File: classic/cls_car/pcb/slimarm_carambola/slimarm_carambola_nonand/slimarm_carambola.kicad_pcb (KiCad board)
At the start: 4 copper layers, 42 x 25.6 mm, 74 parts, among them J1 USB_C_Receptacle_USB2.0, J2 Conn_01x05, J3 Conn_01x04, J4 Conn_01x04, U1 AT91SAM9G25-CU, U2 16bit-DDR2-8bank-FBGA84, U3 W25Q128JVS, U5 XC6206PxxxMR, U6 XC6206PxxxMR, U7 XC6206PxxxMR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

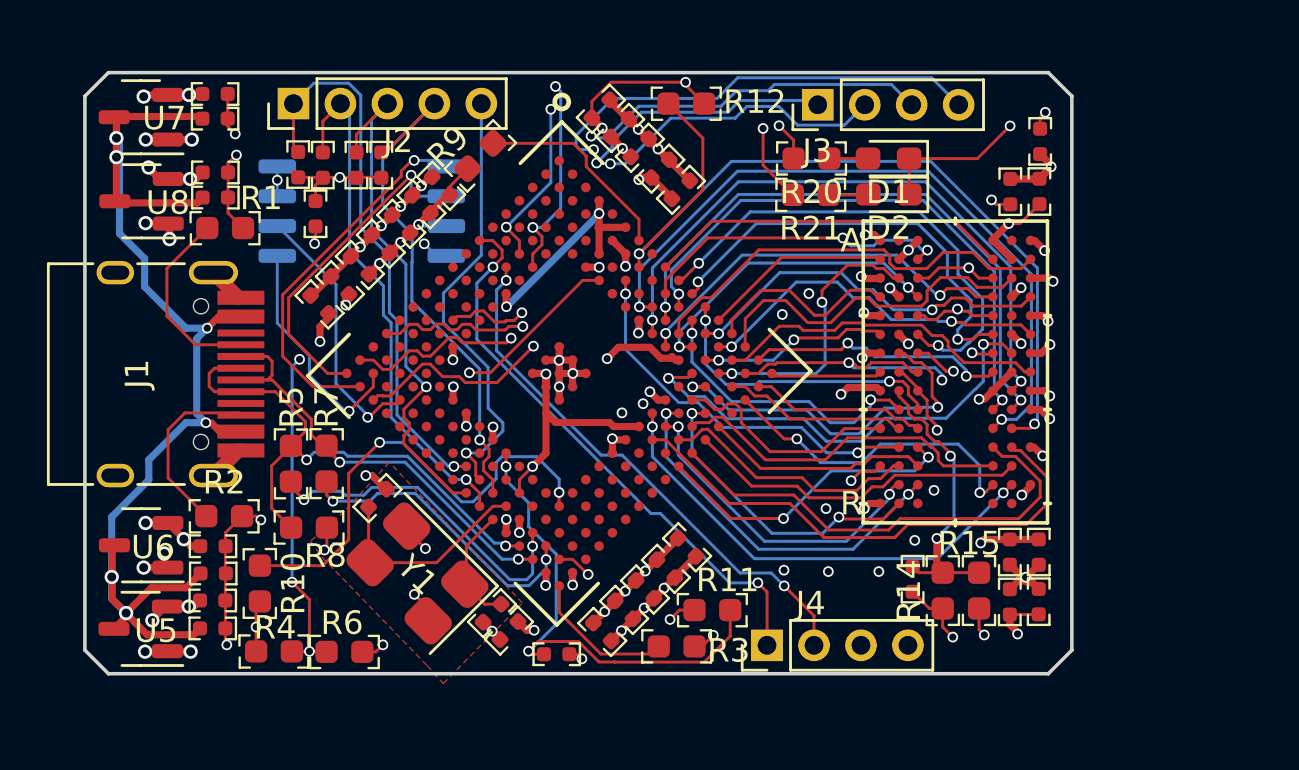
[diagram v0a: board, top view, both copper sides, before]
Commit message: fixed carambola board; board 3d models
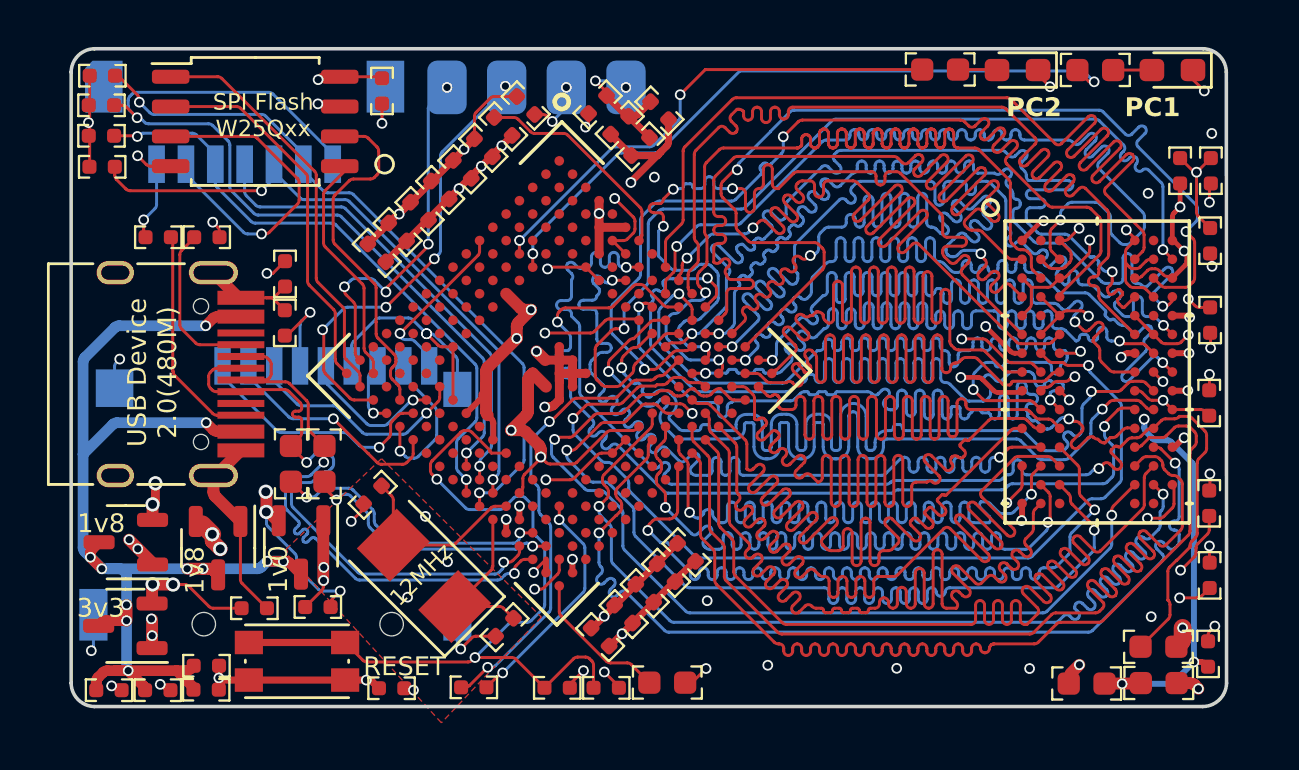
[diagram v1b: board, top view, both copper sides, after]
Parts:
- removed C17, C18: 100nF, jlywxy:0402
- removed J3: Conn_01x04, Connector_PinHeader_2.00mm:PinHeader_1x04_P2.00mm_Vertical
- removed R16, R17, R18, R19: 10k, jlywxy:0402
- removed R4: NC, jlywxy:0603
- removed R6: 0, jlywxy:0603
- removed R8: 1.5k, jlywxy:0603
- added C28: 100nF, jlywxy:0402, F.Cu at (24.9, 25.1)
- added G***: LOGO, jlywxy:image_microchip, B.Cu at (27.6, 20.6)
- added R13: 10k, jlywxy:0402, F.Cu at (17.1, 15.9)
- added R22: 10k, jlywxy:0402, F.Cu at (17.1, 14.6)
- added R23: 10k, jlywxy:0402, F.Cu at (17.1, 18.5)
- added R24: 10k, jlywxy:0402, F.Cu at (17.1, 17.2)
- added SW1: SW_MEC_5E, jlywxy:BUTTON_4P_3x4, F.Cu at (25.4, 39.5)
- added U4: ~, jlywxy:MicroSD-TF_PUSH-SHOUHAN, B.Cu at (33.6, 25.5)
- J2: value Conn_01x05 -> Conn_01x04; footprint Connector_PinHeader_2.00mm:PinHeader_1x05_P2.00mm_Vertical -> Connector_PinHeader_2.54mm:PinHeader_1x04_P2.54mm_Vertical; moved to B.Cu
- J4: value Conn_01x04 -> DF13A-7P-1.25H21; footprint Connector_PinHeader_2.00mm:PinHeader_1x04_P2.00mm_Vertical -> jlywxy:DF13A-7P-1.25H21; moved to B.Cu
- R1, R2, R9: footprint jlywxy:0603 -> jlywxy:0402
- R10, R11: value 1.5k -> 5.1k; footprint jlywxy:0603 -> jlywxy:0402
- U3: moved to F.Cu
- Y1: value Crystal_GND24 -> Crystal; footprint jlywxy:Crystal_5032-4P -> Crystal:Crystal_SMD_5032-2Pin_5.0x3.2mm
- moved R12 30.6 mm to (62.1, 38.9)
- moved G*** 28.2 mm to (20.0, 20.7)
- moved J4 27.6 mm to (26.9, 18.4), turned to 0 degrees
- moved C38 26.4 mm to (29.4, 40.7), turned to 0 degrees
- moved G*** 25.7 mm to (27.7, 23.7)
- moved C39 23.3 mm to (21.6, 39.7)
- moved C37 21.0 mm to (21.6, 40.8)
- moved C40 19.0 mm to (26.3, 37.2), turned to 0 degrees
- moved U7 18.6 mm to (22.1, 34.7), turned to -90 degrees
- moved C24 18.4 mm to (64.3, 35.9)
- moved U8 16.2 mm to (25.6, 34.7), turned to -90 degrees
- moved C19 15.1 mm to (64.3, 21.6)
- moved C11 14.9 mm to (39.2, 16.7), turned to -135 degrees
- moved J2 14.2 mm to (39.4, 15.1)
- moved C20 13.1 mm to (64.3, 25.0)
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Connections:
- net /DDR_CLK renamed /DDR_CLKP
- net /DDR_NCLK renamed /DDR_CLKN
- J2 pad 1: /JTAG_TDI -> GND
- J2 pad 2: /JTAG_TMS -> /3v3
- J2 pad 3: /JTAG_TCK -> /DEBUG_RXD
- J2 pad 4: /JTAG_RST -> /DEBUG_TXD
- J4 pad 1: /UART_UTXD -> /JTAG_TDI
- J4 pad 2: /UART_URXD -> /JTAG_TMS
- J4 pad 3: /3v3 -> /JTAG_RST
- J4 pad 4: GND -> /JTAG_TDO
- R10 pad 2: /3v3 -> /1v8_CPUMEM
- R12 pad 2: /3v3 -> /1v8_DDR
- R15 pad 2: /3v3 -> /1v8_DDR
- U1 pad D7: Net-(U1A-JTAGSEL) -> GND
- U1 pad G1: /UART_UTXD -> /SD_DET
- U1 pad G3: /UART_URXD -> unconnected-(U1A-PC9-PadG3)
- U1 pad L3: /UART_TXD -> unconnected-(U1A-PA0-PadL3)
- U1 pad P1: /UART_RXD -> unconnected-(U1B-PA1-PadP1)
- U1 pad P5: unconnected-(U1B-PA16-PadP5) -> /MCI0_CDA
- U1 pad R5: unconnected-(U1B-PA17-PadR5) -> /MCI0_CK
- U1 pad T5: unconnected-(U1B-PA19-PadT5) -> /MCI0_DA2
- U1 pad U4: unconnected-(U1B-PA15-PadU4) -> /MCI0_DA0
- U1 pad U5: unconnected-(U1B-PA18-PadU5) -> /MCI0_DA1
- U1 pad U6: unconnected-(U1B-PA20-PadU6) -> /MCI0_DA3
- Y1 pad 2: GND -> /XTAL_IN
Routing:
- net /3v3: track 50.9 -> 106.9 mm
- net /DDR_D4: track 4.65 -> 43.9 mm
- net /DDR_BA1: track 7.52 -> 43.8 mm
- net /DDR_BA0: track 7.73 -> 43.8 mm
- net /DDR_D14: track 8.02 -> 43.8 mm
- net /UART_RXD: track 34.3 -> 0.00 mm, vias 2 -> 0
- net /DDR_A5: track 9.59 -> 43.8 mm
- net /DDR_BA2: track 9.86 -> 43.8 mm
- net /DDR_D12: track 8.30 -> 41.2 mm, vias 0 -> 2
- net /DDR_D3: track 12.3 -> 43.8 mm, vias 2 -> 0
- net /DDR_D6: track 8.07 -> 39.4 mm, vias 2 -> 4
- net /DDR_A12: track 13.1 -> 43.6 mm, vias 2 -> 0
- net Net-(U1A-JTAGSEL): track 30.5 -> 0.00 mm, vias 4 -> 0
- net /DDR_D2: track 11.1 -> 41.5 mm
- net /DDR_A3: track 11.1 -> 41.3 mm, vias 0 -> 2
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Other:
- board size 42 x 25.6 mm -> 49.2 x 28 mm
- board text added: "12MHz"
- board text added: "1v0"
- board text added: "1v8"
- board text added: "3v3"
- board text added: "Carambola v1r0x202 AT91SAM9G25@400MHz github: jlywxy/slimarm"
- board text added: "G 3 R T DBGU"
- board text added: "JTAG I M R O C 3 G"
- board text added: "Micro SD DET: PC8"
- board text added: "PC2 PC1"
- board text added: "PCB Impedace Control Stacking: using JLC 3313H 1. DDR_*(ALL length 1737 +-3 mil) * 55 Ohm single-end: 5mil * 100 Ohm differential: 5mil/9mil 2. *DP/*DN * 90 Ohm differential: 5mil/5mil"
- board text added: "RESET"
- board text added: "SPI Flash W25Qxx"
- board text added: "SlimARM Classic"
- board text added: "USB Device 2.0(480M)"
- board text removed: "SlimARM Classic Carambola [Dev]v0r0(23.5.6) github: jlywxy/slimarm"
